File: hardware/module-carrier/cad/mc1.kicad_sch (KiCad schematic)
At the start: 17 parts, among them J1 FUSED ISOLATED 5V INPUT, J2 D24V22F3 external assembled b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, J3 DFR0627 WK2132 ready module h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, J4 ZAC93 ready module harness, J5 CC1101 ready module harness, J6 LD2450 radar harness, J7 BME680 external pod harness, J8 XIAO BOOT service short to GND, U1 ESP32-S3-DevKitC-1-N8R8 v1.1, U2 ESP32-H2-DevKitM-1-N4S, U3 Seeed XIAO MG24 pre-soldered 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, U4 WIZ850io finished module

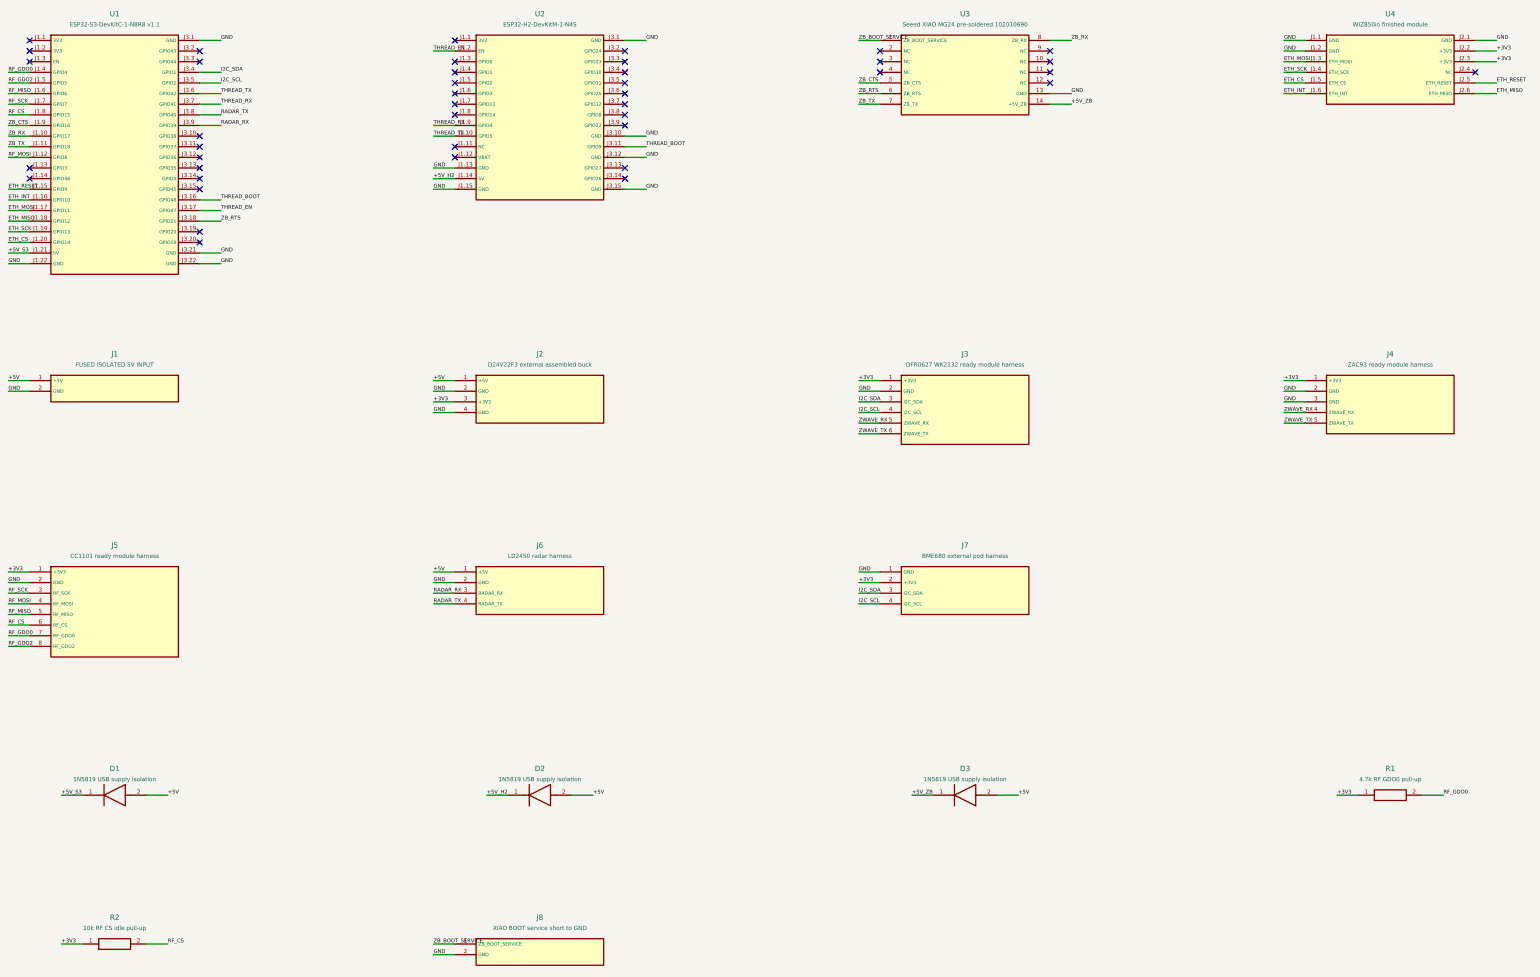
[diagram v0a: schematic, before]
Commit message: Implement compact Nano carrier and bounded Thread recovery
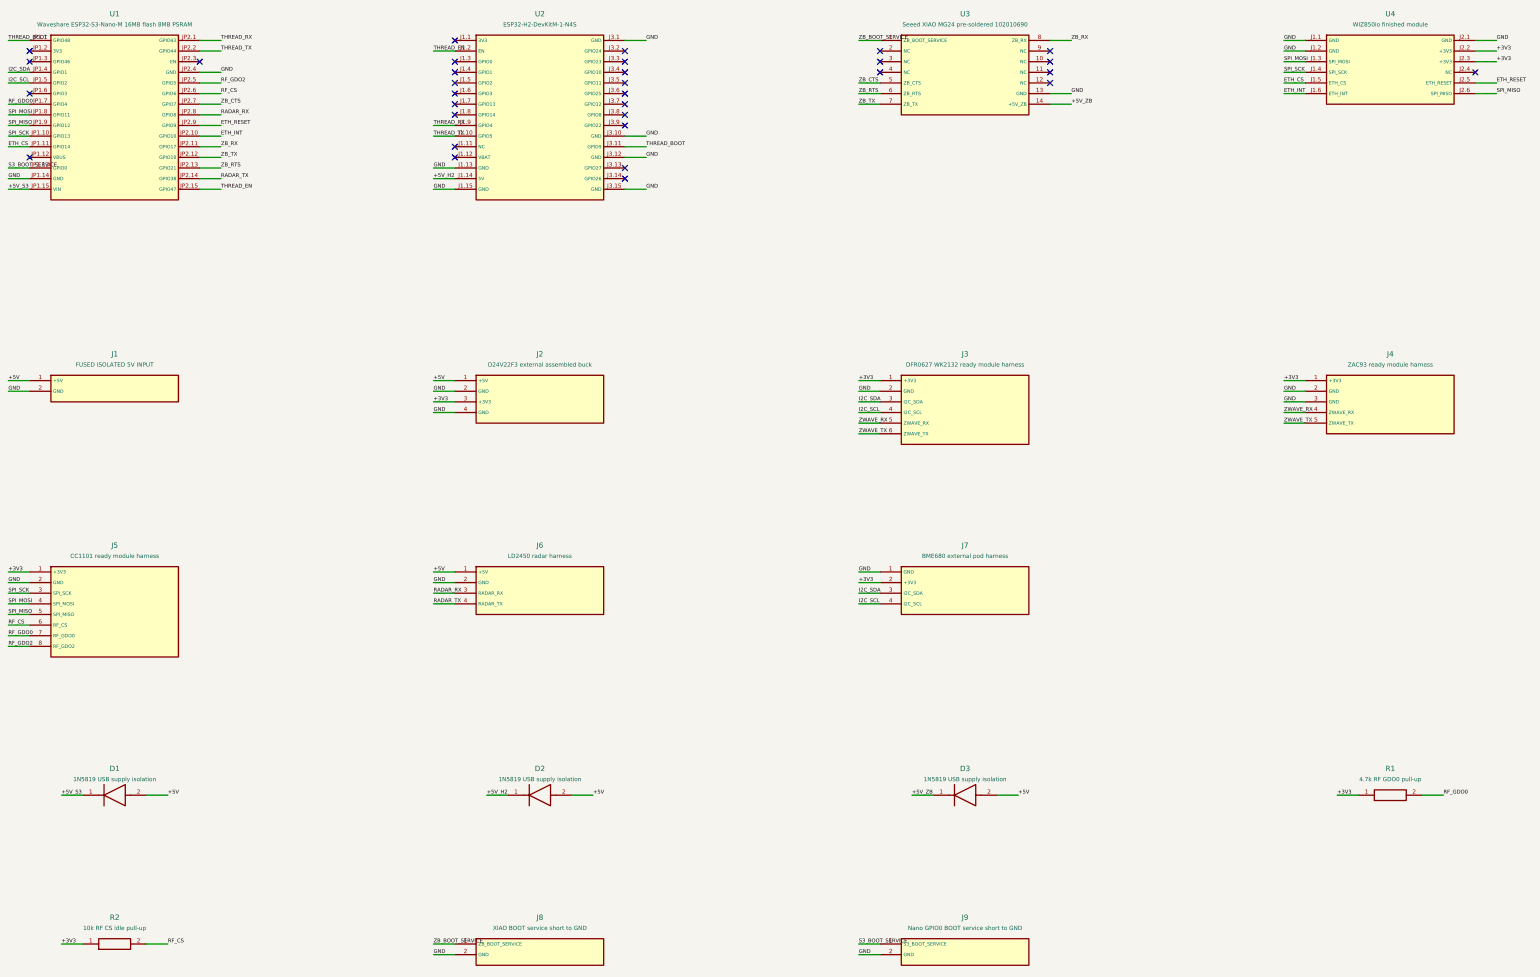
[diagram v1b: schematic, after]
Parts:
- added J9: Nano GPIO0 BOOT service short to GND, MC1:PinHeader_1x02_P2.54mm_Vertical, symbol MC1:Module_J9
- U1: value ESP32-S3-DevKitC-1-N8R8 v1.1 -> Waveshare ESP32-S3-Nano-M 16MB flash 8MB PSRAM; footprint MC1:S3_DevKitC1_v11 -> MC1:S3_Nano_M
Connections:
- net +5V_S3: now also U1.JP1.15 (VIN); no longer U1.J1.21 (5V)
- net ETH_CS: now also U1.JP1.11 (GPIO14); no longer U1.J1.20 (GPIO14)
- net ETH_INT: now also U1.JP2.10 (GPIO10); no longer U1.J1.16 (GPIO10)
- net ETH_RESET: now also U1.JP2.9 (GPIO9); no longer U1.J1.15 (GPIO9)
- net GND: now also U1.JP1.14 (GND), U1.JP2.4 (GND), J9.2 (GND); no longer U1.J1.22 (GND), U1.J3.1 (GND), U1.J3.21 (GND), U1.J3.22 (GND)
- net I2C_SCL: now also U1.JP1.5 (GPIO2); no longer U1.J3.5 (GPIO2)
- net I2C_SDA: now also U1.JP1.4 (GPIO1); no longer U1.J3.4 (GPIO1)
- net RADAR_RX: now also U1.JP2.8 (GPIO8); no longer U1.J3.9 (GPIO39)
- net RADAR_TX: now also U1.JP2.14 (GPIO38); no longer U1.J3.8 (GPIO40)
- net RF_CS: now also U1.JP2.6 (GPIO6); no longer U1.J1.8 (GPIO15)
- net RF_GDO0: now also U1.JP1.7 (GPIO4); no longer U1.J1.4 (GPIO4)
- net RF_GDO2: now also U1.JP2.5 (GPIO5); no longer U1.J1.5 (GPIO5)
- net THREAD_BOOT: now also U1.JP1.1 (GPIO48); no longer U1.J3.16 (GPIO48)
- net THREAD_EN: now also U1.JP2.15 (GPIO47); no longer U1.J3.17 (GPIO47)
- net THREAD_RX: now also U1.JP2.1 (GPIO43); no longer U1.J3.7 (GPIO41)
- net THREAD_TX: now also U1.JP2.2 (GPIO44); no longer U1.J3.6 (GPIO42)
- net ZB_CTS: now also U1.JP2.7 (GPIO7); no longer U1.J1.9 (GPIO16)
- net ZB_RTS: now also U1.JP2.13 (GPIO21); no longer U1.J3.18 (GPIO21)
- net ZB_RX: now also U1.JP2.11 (GPIO17); no longer U1.J1.10 (GPIO17)
- net ZB_TX: now also U1.JP2.12 (GPIO18); no longer U1.J1.11 (GPIO18)
- net ETH_MISO renamed SPI_MISO
- net SPI_MISO: now also J5.5 (SPI_MISO), U1.JP1.9 (GPIO12); no longer U1.J1.18 (GPIO12)
- net ETH_MOSI renamed SPI_MOSI
- net SPI_MOSI: now also J5.4 (SPI_MOSI), U1.JP1.8 (GPIO11); no longer U1.J1.17 (GPIO11)
- net ETH_SCK renamed SPI_SCK
- net SPI_SCK: now also J5.3 (SPI_SCK), U1.JP1.10 (GPIO13); no longer U1.J1.19 (GPIO13)
- removed net RF_MISO: J5.5 (RF_MISO), U1.J1.6 (GPIO6)
- removed net RF_MOSI: J5.4 (RF_MOSI), U1.J1.12 (GPIO8)
- removed net RF_SCK: J5.3 (RF_SCK), U1.J1.7 (GPIO7)
- new net S3_BOOT_SERVICE: J9.1 (S3_BOOT_SERVICE), U1.JP1.13 (GPIO0)
- no-connect marks 42 -> 32
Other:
- title: MC1 - ready-module carrier / engineering prototype -> MC1 Nano - ready-module carrier / engineering prototype

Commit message: Compact MC1 carrier and implement network radio updates
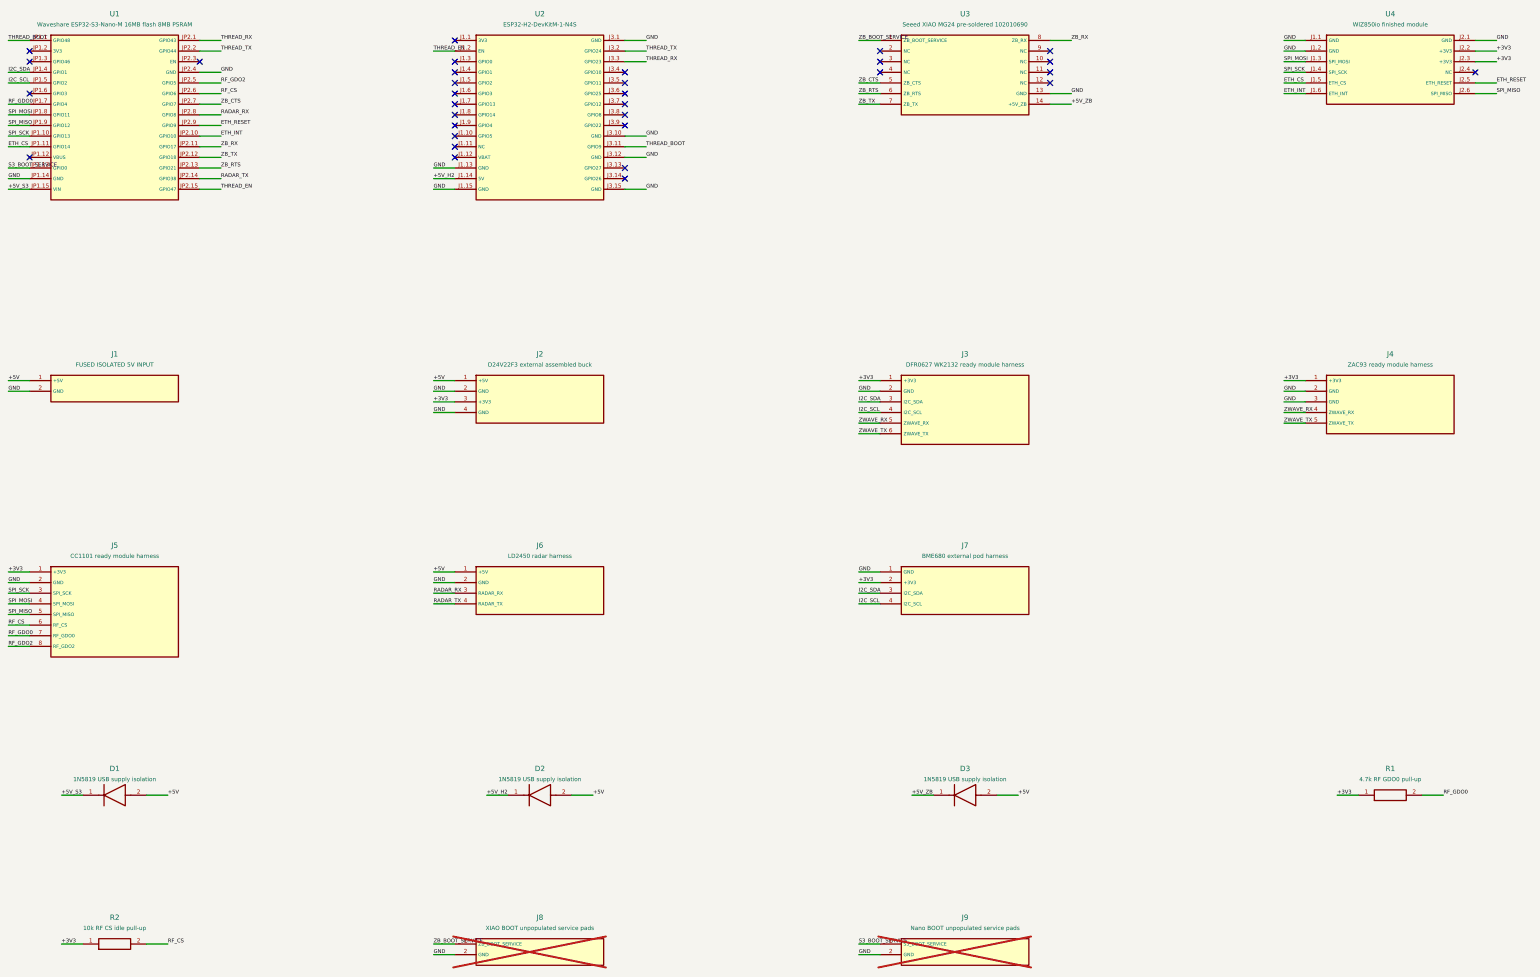
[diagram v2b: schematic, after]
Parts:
- J8: value XIAO BOOT service short to GND -> XIAO BOOT unpopulated service pads; now not fitted
- J9: value Nano GPIO0 BOOT service short to GND -> Nano BOOT unpopulated service pads; now not fitted
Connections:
- net THREAD_RX: now also U2.J3.3 (GPIO23); no longer U2.J1.9 (GPIO4)
- net THREAD_TX: now also U2.J3.2 (GPIO24); no longer U2.J1.10 (GPIO5)
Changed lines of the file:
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@@
 (wire (pts (xy 66.04 66.04) (xy 71.12 66.04)) (stroke (width 0) (type default)))
 (wire (pts (xy 127.0 33.02) (xy 121.92 33.02)) (stroke (width 0) (type default)))
-(wire (pts (xy 127.0 50.8) (xy 121.92 50.8)) (stroke (width 0) (type default)))
-(wire (pts (xy 127.0 53.34) (xy 121.92 53.34)) (stroke (width 0) (type default)))
 (wire (pts (xy 127.0 60.96) (xy 121.92 60.96)) (stroke (width 0) (type default)))
 (wire (pts (xy 127.0 63.5) (xy 121.92 63.5)) (stroke (width 0) (type default)))
 (wire (pts (xy 127.0 66.04) (xy 121.92 66.04)) (stroke (width 0) (type default)))
 (wire (pts (xy 167.64 30.48) (xy 172.72 30.48)) (stroke (width 0) (type default)))
+(wire (pts (xy 167.64 33.02) (xy 172.72 33.02)) (stroke (width 0) (type default)))
+(wire (pts (xy 167.64 35.56) (xy 172.72 35.56)) (stroke (width 0) (type default)))
 (wire (pts (xy 167.64 53.34) (xy 172.72 53.34)) (stroke (width 0) (type default)))
 (wire (pts (xy 167.64 55.88) (xy 172.72 55.88)) (stroke (width 0) (type default)))
@@
 (label "THREAD_EN" (at 71.12 66.04 0) (effects (font (size 0.9 0.9)) (justify left bottom)))
 (label "THREAD_EN" (at 121.92 33.02 180) (effects (font (size 0.9 0.9)) (justify left bottom)))
-(label "THREAD_RX" (at 121.92 50.8 180) (effects (font (size 0.9 0.9)) (justify left bottom)))
-(label "THREAD_TX" (at 121.92 53.34 180) (effects (font (size 0.9 0.9)) (justify left bottom)))
 (label "GND" (at 121.92 60.96 180) (effects (font (size 0.9 0.9)) (justify left bottom)))
 (label "+5V_H2" (at 121.92 63.5 180) (effects (font (size 0.9 0.9)) (justify left bottom)))
 (label "GND" (at 121.92 66.04 180) (effects (font (size 0.9 0.9)) (justify left bottom)))
 (label "GND" (at 172.72 30.48 0) (effects (font (size 0.9 0.9)) (justify left bottom)))
+(label "THREAD_TX" (at 172.72 33.02 0) (effects (font (size 0.9 0.9)) (justify left bottom)))
+(label "THREAD_RX" (at 172.72 35.56 0) (effects (font (size 0.9 0.9)) (justify left bottom)))
 (label "GND" (at 172.72 53.34 0) (effects (font (size 0.9 0.9)) (justify left bottom)))
 (label "THREAD_BOOT" (at 172.72 55.88 0) (effects (font (size 0.9 0.9)) (justify left bottom)))
@@
 (no_connect (at 127.0 45.72))
 (no_connect (at 127.0 48.26))
+(no_connect (at 127.0 50.8))
+(no_connect (at 127.0 53.34))
 (no_connect (at 127.0 55.88))
 (no_connect (at 127.0 58.42))
-(no_connect (at 167.64 33.02))
-(no_connect (at 167.64 35.56))
 (no_connect (at 167.64 38.1))
 (no_connect (at 167.64 40.64))
@@
 (pin "2")
 (instances (project "mc1" (path "/8d5aba07-b883-5616-ab6b-74aeee708de7" (reference "R2") (unit 1)))))
-(symbol (lib_id "MC1:Module_J8") (at 147.3200 246.3800 0) (unit 1) (in_bom yes) (on_board yes) (dnp no)
+(symbol (lib_id "MC1:Module_J8") (at 147.3200 246.3800 0) (unit 1) (in_bom yes) (on_board yes) (dnp yes)
 (property "Reference" "J8" (at 147.32 240.03 0) (effects (font (size 1.27 1.27))))
-(property "Value" "XIAO BOOT service short to GND" (at 147.32 242.57 0) (effects (font (size 1 1))))
+(property "Value" "XIAO BOOT unpopulated service pads" (at 147.32 242.57 0) (effects (font (size 1 1))))
 (property "Footprint" "MC1:PinHeader_1x02_P2.54mm_Vertical" (at 147.32 246.38 0) (effects (font (size 1 1)) hide))
 (pin "1")
 (pin "2")
 (instances (project "mc1" (path "/8d5aba07-b883-5616-ab6b-74aeee708de7" (reference "J8") (unit 1)))))
-(symbol (lib_id "MC1:Module_J9") (at 248.9200 246.3800 0) (unit 1) (in_bom yes) (on_board yes) (dnp no)
+(symbol (lib_id "MC1:Module_J9") (at 248.9200 246.3800 0) (unit 1) (in_bom yes) (on_board yes) (dnp yes)
 (property "Reference" "J9" (at 248.92 240.03 0) (effects (font (size 1.27 1.27))))
-(property "Value" "Nano GPIO0 BOOT service short to GND" (at 248.92 242.57 0) (effects (font (size 1 1))))
+(property "Value" "Nano BOOT unpopulated service pads" (at 248.92 242.57 0) (effects (font (size 1 1))))
 (property "Footprint" "MC1:PinHeader_1x02_P2.54mm_Vertical" (at 248.92 246.38 0) (effects (font (size 1 1)) hide))
 (pin "1")
